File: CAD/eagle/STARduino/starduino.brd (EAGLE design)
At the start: 101.6 x 38.1 mm, 114 parts, among them J1 J30J-9J30, J2 MICRO_SD, J3 J30J-15J30, J4 J30J-31J30, J5 RPI-ZERO, J6 RPI-CSI, Q1 BSS8402DW, Q2 BSS8402DW, Q3 BSS8402DW, T1 750313975, U1 LT8301, U10 MC14504BDTG, U11 MAX31725MTA+, U12 TCA9535_RTW_24, U13 BMX055, U14 DRV8846RGER, U15 MC74VHC1GT125, U16 PCA9515A, U17 PCA9306DCT, U2 LT3465/A, U3 LTC3112FE, U4 DS3231MZ+, U5 MT25QL01GBBB8ESF-0AAT, U6 ATSAMD21G18, U7 MIC5319, U8 ADXL375BCCZ, U9 MC74VHC1GT125

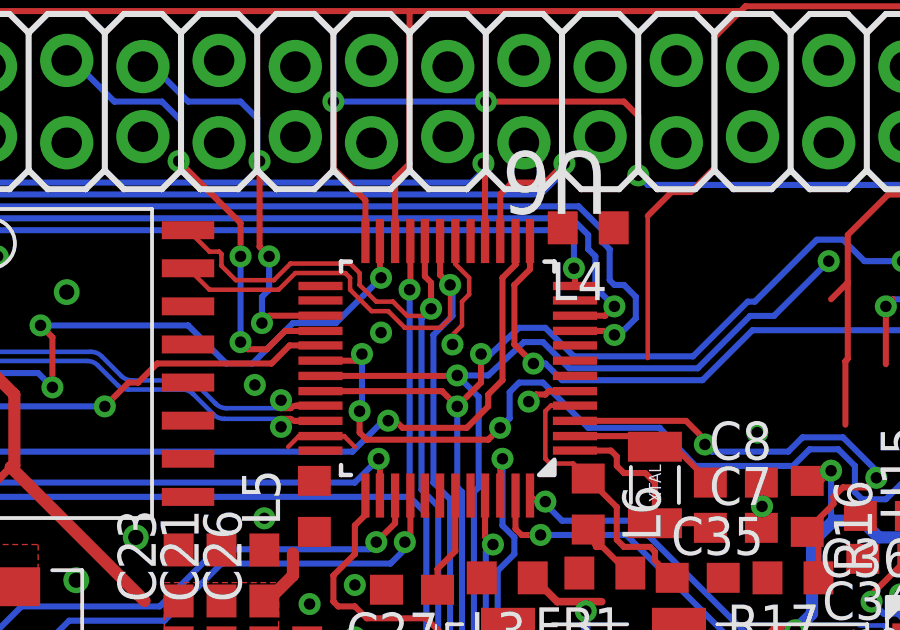
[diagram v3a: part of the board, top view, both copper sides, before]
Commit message: Fixed SERCOMS.
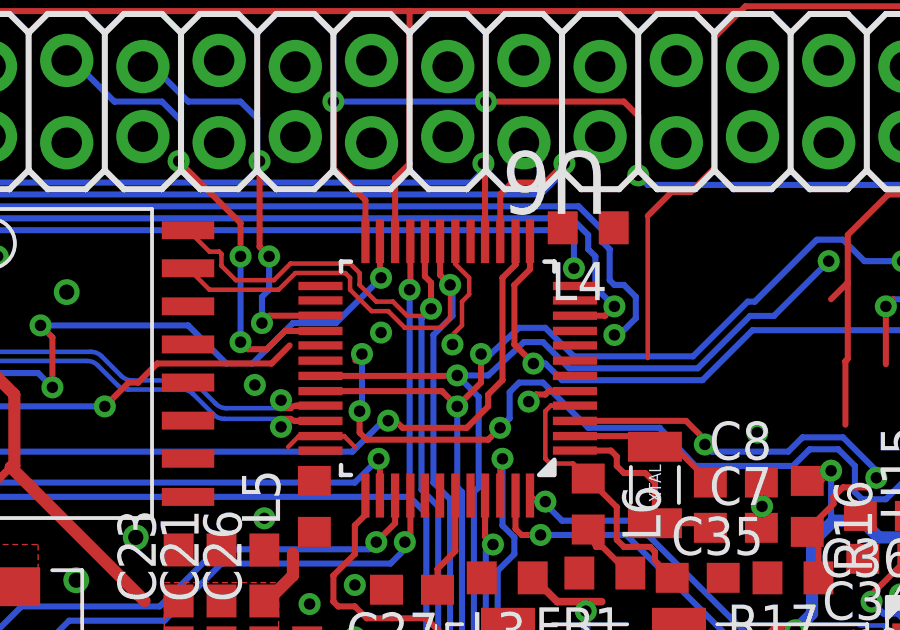
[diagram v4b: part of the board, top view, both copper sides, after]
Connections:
- net IOEINT: now also U6.26; no longer U6.30
- net PI_KILL: now also U6.25; no longer U6.29
- net RX2: now also U6.30; no longer U6.12
- net TX2: now also U6.29; no longer U6.9
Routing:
- net TX2: track 68.3 -> 67.1 mm
- net IOEINT: track 28.3 -> 27.1 mm
- net PI_KILL: track 23.4 -> 22.4 mm
- net RX2: track 62.2 -> 61.6 mm
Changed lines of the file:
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@@
 <?xml version="1.0" encoding="utf-8"?>
 <!DOCTYPE eagle SYSTEM "eagle.dtd">
-<eagle version="6.5.0">
+<eagle version="7.7.0">
 <drawing>
 <settings>
@@
 <pass name="Default">
 <param name="RoutingGrid" value="50mil"/>
+<param name="AutoGrid" value="1"/>
+<param name="Efforts" value="0"/>
+<param name="TopRouterVariant" value="1"/>
 <param name="tpViaShape" value="round"/>
 <param name="PrefDir.1" value="|"/>
@@
 <signal name="IOEINT">
 <contactref element="U15" pad="4"/>
-<contactref element="U6" pad="30"/>
 <wire x1="70.140625" y1="22.051875" x2="69.75625" y2="22.051875" width="0.2032" layer="1"/>
 <wire x1="69.75625" y1="22.051875" x2="69.37375" y2="21.669375" width="0.2032" layer="1"/>
@@
 <via x="50.4825" y="25.87625" extent="1-16" drill="0.381"/>
 <wire x1="50.4825" y1="25.87625" x2="50.26025" y2="25.654" width="0.2032" layer="1"/>
-<wire x1="50.26025" y1="25.654" x2="49.0982" y2="25.654" width="0.2032" layer="1"/>
 <wire x1="50.64125" y1="23.01875" x2="54.689375" y2="23.01875" width="0.2032" layer="1"/>
 <wire x1="54.689375" y1="23.01875" x2="55.08625" y2="23.415625" width="0.2032" layer="1"/>
@@
 <wire x1="56.515" y1="24.92375" x2="58.023125" y2="23.415625" width="0.2032" layer="16"/>
 <wire x1="58.023125" y1="23.415625" x2="60.404375" y2="23.415625" width="0.2032" layer="16"/>
+<contactref element="U6" pad="26"/>
+<wire x1="50.4825" y1="25.87625" x2="49.0982" y2="27.6606" width="0" layer="19" extent="1-1"/>
 </signal>
 <signal name="N$23">
@@
 </signal>
 <signal name="TX2">
-<contactref element="U6" pad="9"/>
 <contactref element="J3" pad="10"/>
 <via x="58.89625" y="26.51125" extent="1-16" drill="0.381"/>
@@
 <wire x1="4.7625" y1="21.669375" x2="4.7625" y2="23.6475" width="0.2032" layer="1"/>
 <wire x1="4.7625" y1="23.6475" x2="4.28" y2="24.13" width="0.2032" layer="1"/>
-<wire x1="57.5818" y1="26.6446" x2="58.7629" y2="26.6446" width="0.2032" layer="1"/>
 <wire x1="58.7629" y1="26.6446" x2="58.89625" y2="26.51125" width="0.2032" layer="1"/>
 <wire x1="59.610625" y1="27.78125" x2="59.610625" y2="27.066875" width="0.2032" layer="16"/>
 <wire x1="59.610625" y1="27.066875" x2="59.055" y2="26.51125" width="0.2032" layer="16"/>
 <wire x1="59.055" y1="26.51125" x2="58.89625" y2="26.51125" width="0.2032" layer="16"/>
+<contactref element="U6" pad="29"/>
+<wire x1="58.7629" y1="26.6446" x2="49.0982" y2="26.162" width="0" layer="19" extent="1-1"/>
 </signal>
 <signal name="RX2">
-<contactref element="U6" pad="12"/>
 <contactref element="J3" pad="9"/>
-<wire x1="57.5818" y1="28.1432" x2="57.5818" y2="28.698825" width="0.2032" layer="1"/>
 <wire x1="57.5818" y1="28.698825" x2="57.546875" y2="28.73375" width="0.2032" layer="1"/>
 <via x="57.546875" y="28.73375" extent="1-16" drill="0.381"/>
@@
 <wire x1="4.206875" y1="21.510625" x2="4.206875" y2="21.733125" width="0.2032" layer="1"/>
 <wire x1="4.206875" y1="21.733125" x2="3.08" y2="22.86" width="0.2032" layer="1"/>
+<contactref element="U6" pad="30"/>
+<wire x1="57.546875" y1="28.73375" x2="49.0982" y2="25.654" width="0" layer="19" extent="1-1"/>
 </signal>
 <signal name="DEC0">
@@
 <signal name="PI_KILL">
 <contactref element="R11" pad="1"/>
-<contactref element="U6" pad="29"/>
-<wire x1="49.0982" y1="26.162" x2="48.0695" y2="26.162" width="0.2032" layer="1"/>
 <wire x1="28.336875" y1="21.21625" x2="28.36" y2="21.21625" width="0.2032" layer="1"/>
 <wire x1="33.81375" y1="21.9075" x2="34.29" y2="22.38375" width="0.2032" layer="1"/>
@@
 <wire x1="48.0695" y1="26.162" x2="47.46625" y2="25.55875" width="0.2032" layer="1"/>
 <contactref element="Q1" pad="2"/>
-<wire x1="28.336875" y1="21.21625" x2="-10.16" y2="-64.4" width="0" layer="19" extent="1-1"/>
+<contactref element="U6" pad="25"/>
+<wire x1="48.0695" y1="26.162" x2="49.0982" y2="28.1432" width="0" layer="19" extent="1-1"/>
+<wire x1="-10.16" y1="-64.4" x2="28.336875" y2="21.21625" width="0" layer="19" extent="1-1"/>
 </signal>
 <signal name="N$38">

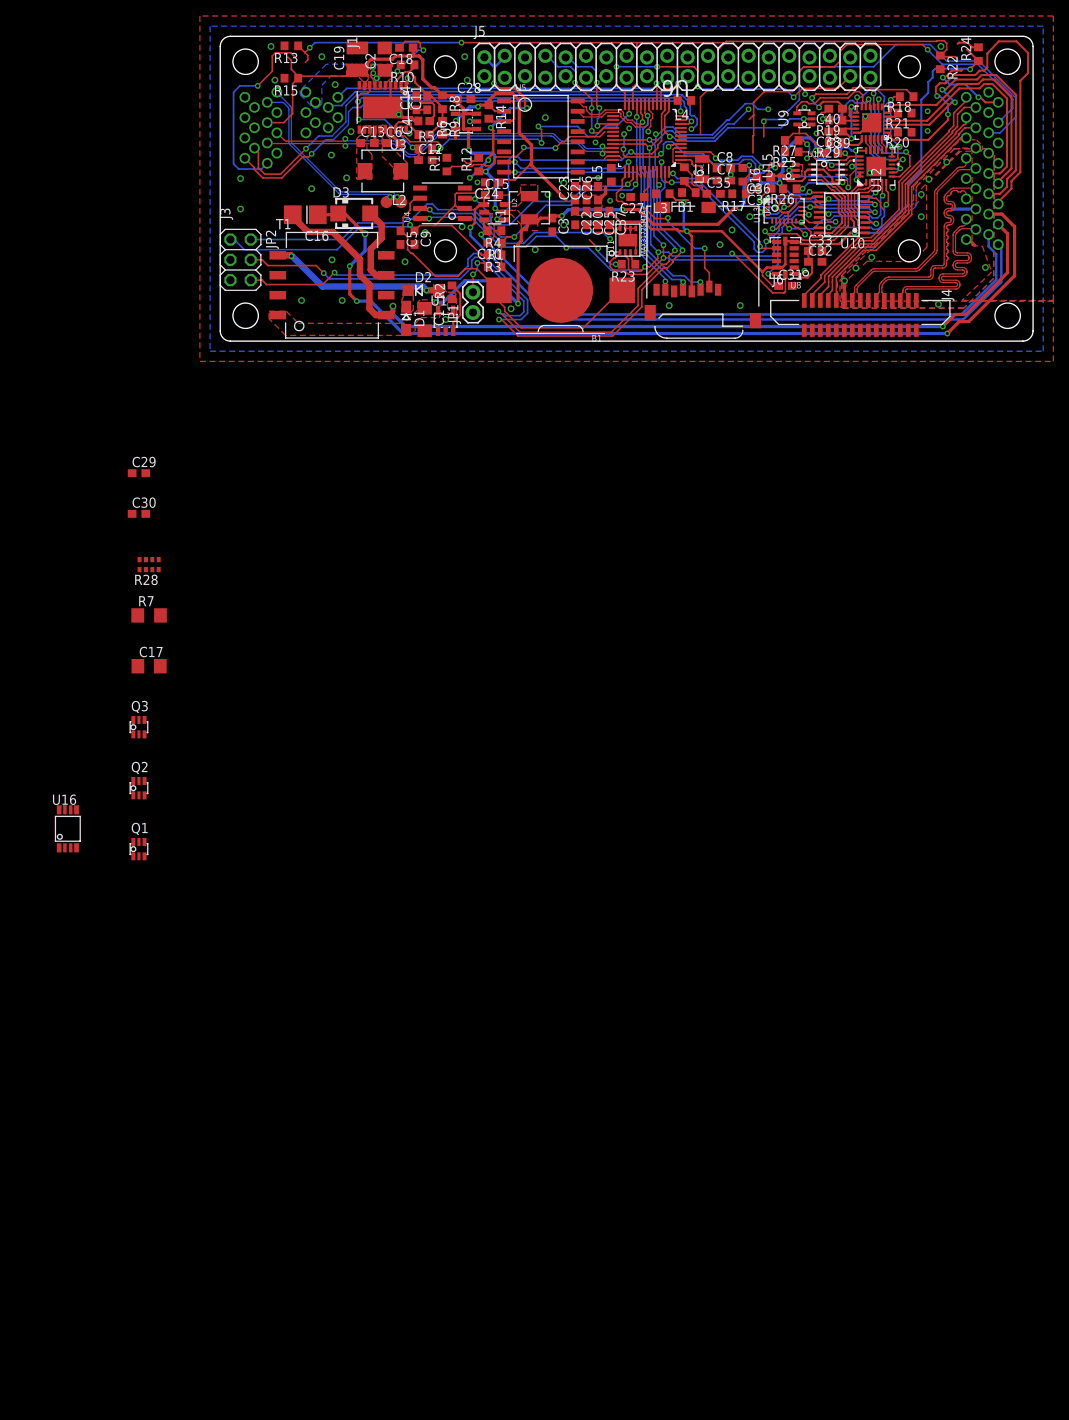
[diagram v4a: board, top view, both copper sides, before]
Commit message: Finished schematic changes
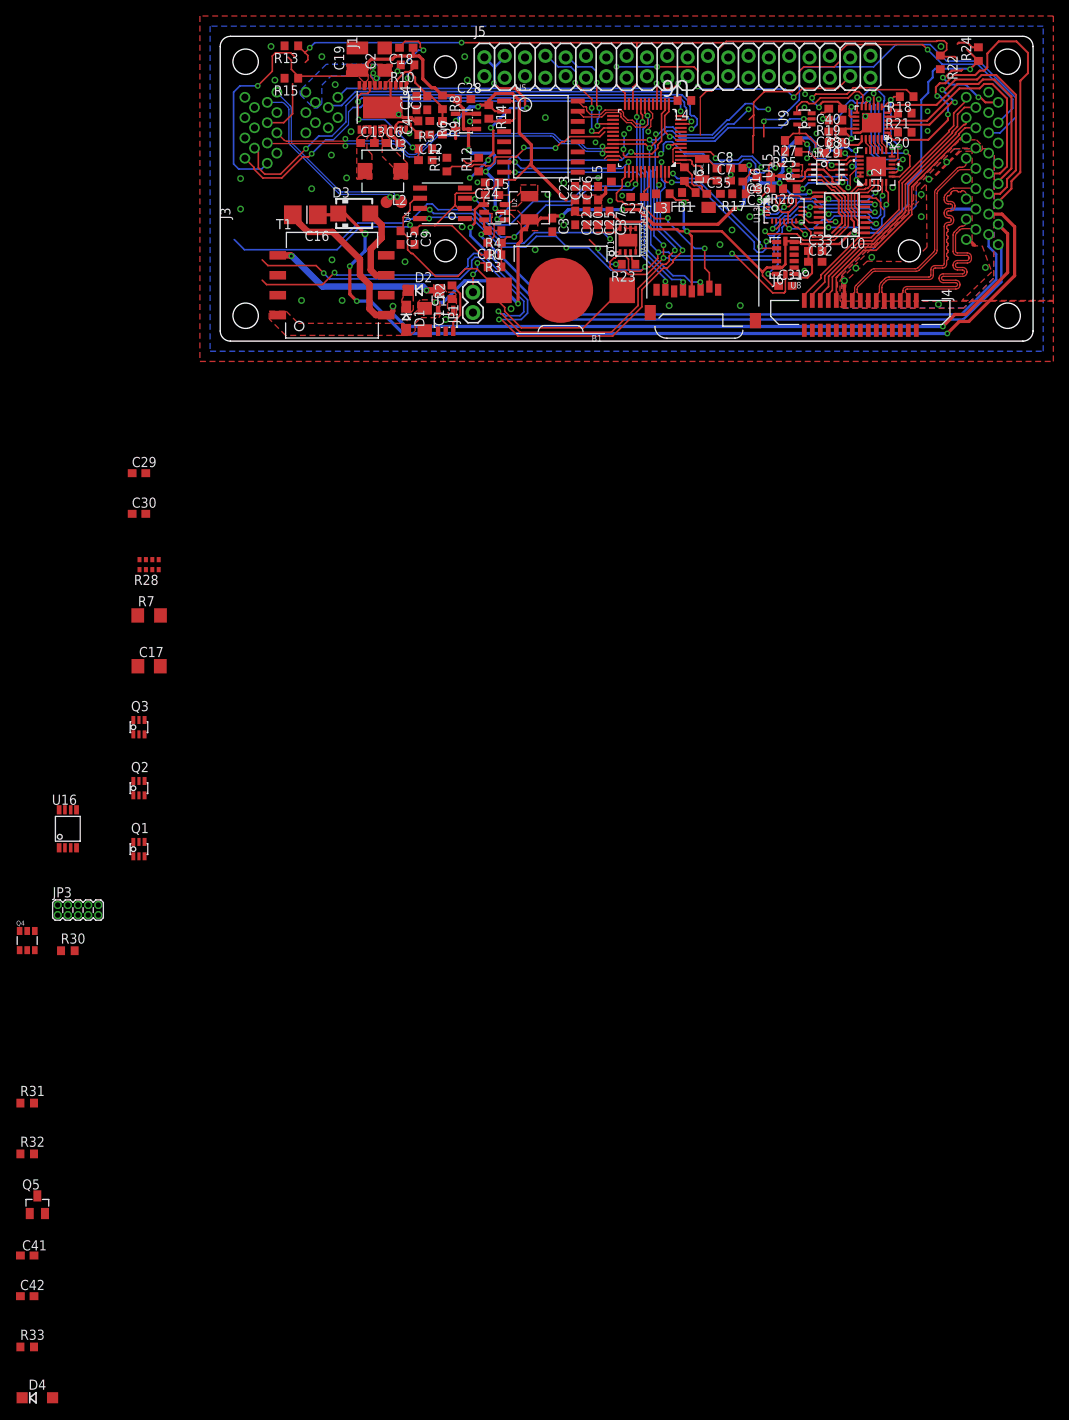
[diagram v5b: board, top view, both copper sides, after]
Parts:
- removed JP2: (no value), pinhead:2X03
- added C41: 100pF, rcl:C0603
- added C42: 1uF, resistor:C0603
- added D4: B0520LW-7-F, CM_diodes:SOD123
- added JP3: (no value), pinhead:2X5/90-50MIL
- added Q4: DMMT5401, transistor-pnp:SOT-26
- added Q5: DMG2305UX, transistor-fet:SOT23
- added R30, R31: 10k, resistor:R0603
- added R32: 47k, resistor:R0603
- added R33: 1M, resistor:R0603
- C11: value 22pF -> 10pF
- C2: value 10uF -> 22uF
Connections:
- removed net COMP_5: C11.1, C14.1, U3.2
- removed net N$46: C14.2, R6.1
- removed net PWM/SYNC: U3.19, U6.23
- new net N$1: Q4.4, Q5.1, R32.2
- new net N$11: C14.1, R6.1
- new net N$12: C11.1, R6.2, U3.2
- new net N$2: Q4.1, Q4.2, Q4.3, R31.2
- new net N$3: R33.1, U3.19
- new net P$1: C28.1, C39.1, C40.1, Q1.4, Q2.4, Q4.5, Q5.3, R12.1, R15.1, R25.2, R26.2, R27.2, R29.2, U10.16, U12.18, U12.21, U12.23, U12.24, U14.15, U7.1, U7.3
- net +3V3: now also JP3.1, R30.2; no longer JP2.1
- net +5V: now also D4.A, Q4.6, Q5.2; no longer C28.1, C39.1, C40.1, Q1.4, Q2.4, R12.1, R15.1, R25.2, R26.2, R27.2, R29.2, U10.16, U12.18, U12.21, U12.23, U12.24, U14.15, U7.1, U7.3
- net EN_28V: now also U6.7
- net FB_5: now also C14.2; no longer R6.2
- net GND: now also C41.2, C42.2, JP3.3, JP3.5, R31.1, R32.1; no longer JP2.5
- net N$35: now also C41.1
- net N$43: now also D4.C, R33.2
- net RESET: now also JP3.10; no longer JP2.2
- net SWDCLK: now also JP3.4, R30.1; no longer JP2.4
- net SWDIO: now also JP3.2; no longer JP2.6
- net VCC: now also C42.1
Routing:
- net PWM/SYNC: track 36.3 -> 0.00 mm, vias 4 -> 0
- net +5V: track 201.2 -> 185.4 mm
- net RESET: track 61.2 -> 49.8 mm
- net COMP_5: track 5.70 -> 0.00 mm
- net N$46: track 5.14 -> 0.00 mm
- net P$1: track 0.00 -> 3.61 mm
- net FB_5: track 14.2 -> 11.1 mm
- net SWDIO: track 88.7 -> 87.3 mm
- net SWDCLK: track 83.9 -> 82.5 mm

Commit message: New starduino routing done
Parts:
- moved C41 167.3 mm to (69.2, 24.5), turned to 90 degrees
- moved R33 158.1 mm to (26.1, 24.1)
- moved D4 158.0 mm to (16.5, 21.0), turned to 270 degrees
- moved C42 152.7 mm to (9.29, 29.6), turned to 270 degrees
- moved Q5 139.2 mm to (28.2, 21.6), flipped to the bottom
- moved Q3 132.9 mm to (92.6, 36.1), turned to 270 degrees
- moved R32 131.8 mm to (29.6, 18.7), flipped to the bottom
- moved R31 124.6 mm to (29.4, 17.3), flipped to the bottom
- moved U16 122.0 mm to (64.0, 28.5), turned to 270 degrees
- moved Q4 106.2 mm to (25.0, 19.2), flipped to the bottom
- moved Q1 94.7 mm to (30.3, 22.1)
- moved Q2 92.8 mm to (8.89, 34.9), turned to 180 degrees
- moved R30 91.9 mm to (12.6, 10.1), flipped to the bottom, turned to 90 degrees
- moved R28 90.4 mm to (64.0, 25.6), turned to 180 degrees
- moved JP3 83.8 mm to (2.54, 10.2), turned to 90 degrees
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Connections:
- removed net P$1: C28.1, C39.1, C40.1, Q1.4, Q2.4, Q4.5, Q5.3, R12.1, R15.1, R25.2, R26.2, R27.2, R29.2, U10.16, U12.18, U12.21, U12.23, U12.24, U14.15, U7.1, U7.3
- new net 5V_S: C28.1, C3.1, C39.1, C40.1, L1.P$1, Q1.4, Q4.5, Q5.3, R12.1, R16.1, R18.1, R19.1, R25.2, R26.2, R27.2, R29.2, U10.16, U12.18, U12.21, U12.23, U12.24, U14.15, U2.5, U7.1, U7.3, U9.5
- new net N$13: C20.1, L3.2, U6.44
- new net N$24: C23.1, C26.1, L4.2, U6.36
- new net N$4: C25.1, L5.2, U6.17
- net +5V: now also Q2.4, R15.1; no longer C3.1, L1.P$1, R16.1, R18.1, R19.1, U2.5, U9.5
- net EN_28V: now also U6.41; no longer U6.7
- net GND: now also J3.14, U16.P$4
- net N$10: no longer C20.1, C23.1, C25.1, C26.1, L3.2, L4.2, L5.2, U6.17, U6.36, U6.44
- net SCL: now also R28.3, U16.P$2; no longer R28.4
- net SCL_BUFF: now also U16.P$7
- net SDA: now also R28.4, U16.P$3; no longer R28.3
- net SDA_BUFF: now also U16.P$6
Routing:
- net 5V_S: track 0.00 -> 153.1 mm, vias 0 -> 16
- net +5V: track 185.4 -> 90.1 mm, vias 17 -> 4
- net EN_28V: track 0.00 -> 46.2 mm, vias 0 -> 4
- net +3V3: track 224.5 -> 258.4 mm, vias 11 -> 15
- net N$43: track 4.63 -> 23.0 mm, vias 0 -> 2
- net RESET: track 49.8 -> 63.0 mm
- net N$4: track 0.00 -> 11.0 mm, vias 0 -> 2
- net SWDCLK: track 82.5 -> 91.8 mm, vias 4 -> 3
- net BIAS_GND: track 109.3 -> 118.3 mm, vias 2 -> 3
- net N$12: track 0.00 -> 8.57 mm, vias 0 -> 2
- net N$1: track 0.00 -> 8.14 mm
- net TX2: track 67.1 -> 59.2 mm
- net N$24: track 0.00 -> 7.20 mm
- net N$35: track 7.02 -> 14.0 mm, vias 2 -> 3
- net N$13: track 0.00 -> 6.90 mm
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- added copper zone on layer 1, net 5V_S
- removed copper zone on layer 1, net +3V3
